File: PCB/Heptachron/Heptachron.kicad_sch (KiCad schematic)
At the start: 37 parts, among them SW1 SW_Push, SW2 SW_Push, U6 BQ24230RGT, U7 IS31FL3729, U8 ATtiny424-SS, X1 RV-3028-C7

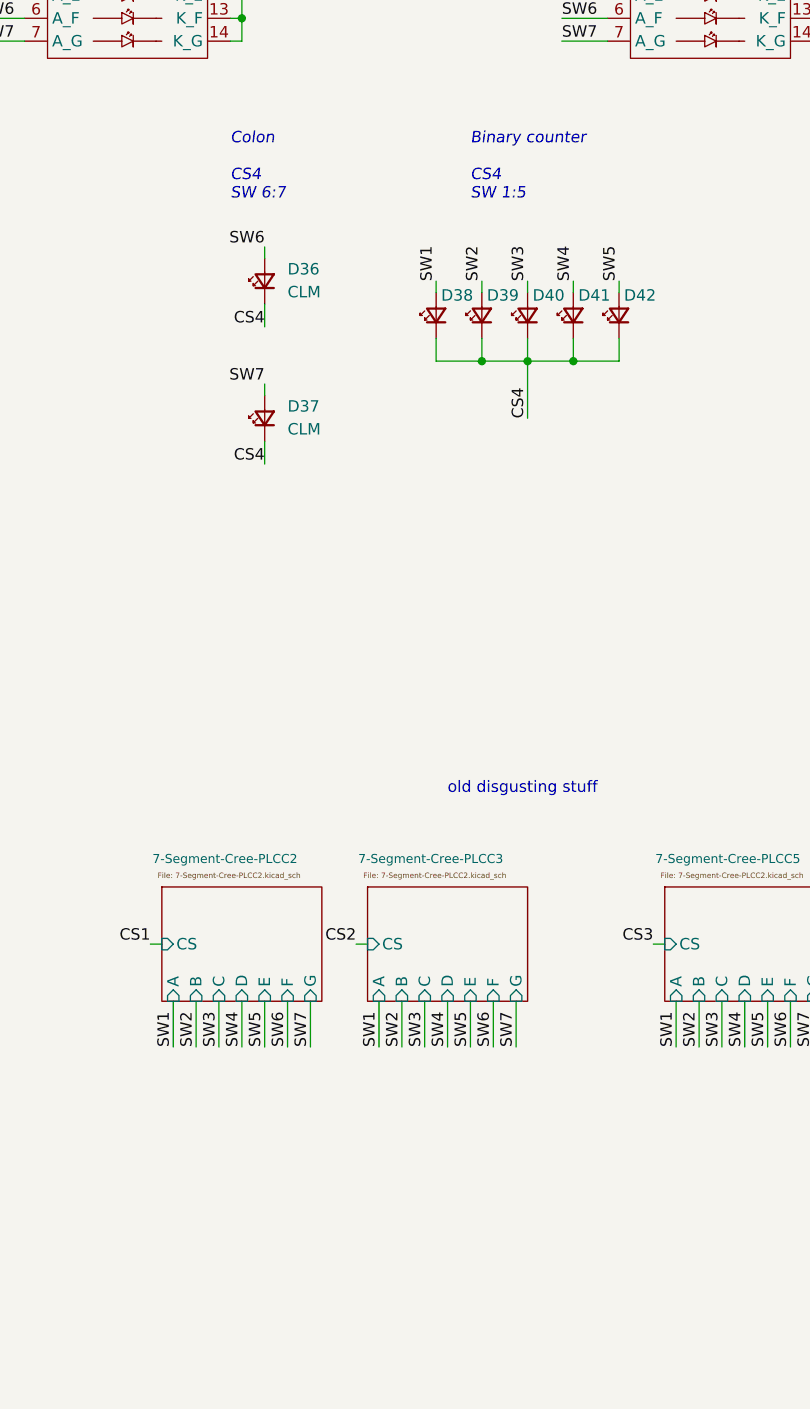
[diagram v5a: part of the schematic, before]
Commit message: Finish test PCB [Ordered]
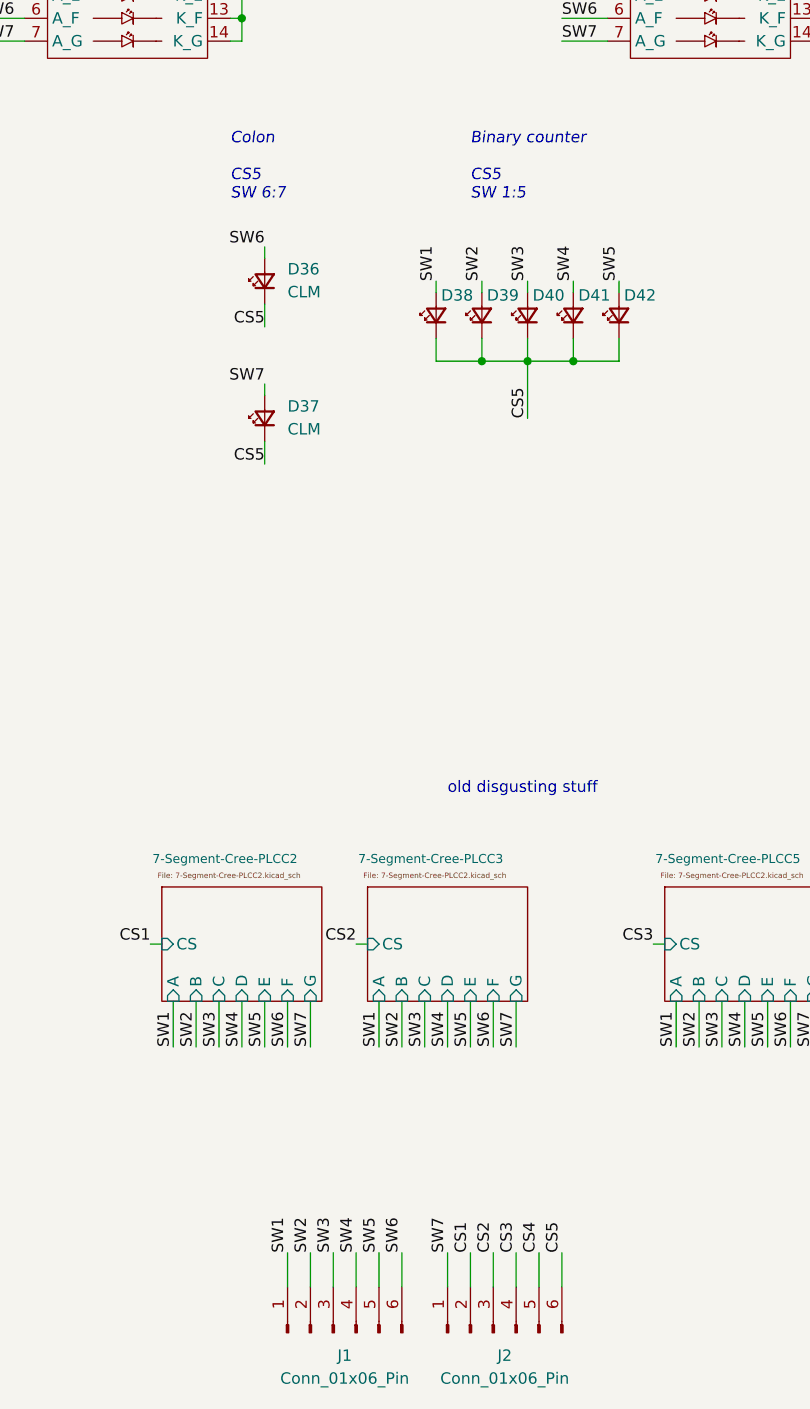
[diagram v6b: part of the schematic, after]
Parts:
- added J1, J2: Conn_01x06_Pin, Connector_Wire:SolderWire-0.1sqmm_1x06_P3.6mm_D0.4mm_OD1mm_Relief, symbol Connector:Conn_01x06_Pin
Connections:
- net CS1: now also J2.2 (Pin_2)
- net CS2: now also J2.3 (Pin_3)
- net CS3: now also J2.4 (Pin_4)
- net CS4: now also J2.5 (Pin_5); no longer D36.1 (K), D37.1 (K), D38.1 (K), D39.1 (K), D40.1 (K), D41.1 (K), D42.1 (K)
- net CS5: now also D36.1 (K), D37.1 (K), D38.1 (K), D39.1 (K), D40.1 (K), D41.1 (K), D42.1 (K), J2.6 (Pin_6)
- net SW1: now also J1.1 (Pin_1)
- net SW2: now also J1.2 (Pin_2)
- net SW3: now also J1.3 (Pin_3)
- net SW4: now also J1.4 (Pin_4)
- net SW5: now also J1.5 (Pin_5)
- net SW6: now also J1.6 (Pin_6)
- net SW7: now also J2.1 (Pin_1)
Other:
- note added: "Binary counter CS5 SW 1:5"
- note added: "Colon CS5 SW 6:7"
- note removed: "Binary counter CS4 SW 1:5"
- note removed: "Colon CS4 SW 6:7"
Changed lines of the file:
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@@
+    (stroke (width 0) (type default))
+  )
+  (wire (pts (xy 311.15 231.14) (xy 311.15 234.95))
     (stroke (width 0) (type default))
   )
@@
     (stroke (width 0) (type default))
   )
+  (wire (pts (xy 331.47 231.14) (xy 331.47 234.95))
+    (stroke (width 0) (type default))
+  )
   (wire (pts (xy 256.54 96.52) (xy 255.27 96.52))
     (stroke (width 0) (type default))
@@
     (stroke (width 0) (type default))
   )
+  (wire (pts (xy 300.99 231.14) (xy 300.99 234.95))
+    (stroke (width 0) (type default))
+  )
   (wire (pts (xy 295.91 91.44) (xy 295.91 93.98))
     (stroke (width 0) (type default))
@@
     (stroke (width 0) (type default))
   )
+  (wire (pts (xy 318.77 231.14) (xy 318.77 234.95))
+    (stroke (width 0) (type default))
+  )
   (wire (pts (xy 295.91 81.28) (xy 295.91 83.82))
     (stroke (width 0) (type default))
@@
     (stroke (width 0) (type default))
   )
+  (wire (pts (xy 303.53 231.14) (xy 303.53 234.95))
+    (stroke (width 0) (type default))
+  )
   (wire (pts (xy 379.73 203.2) (xy 379.73 208.28))
     (stroke (width 0) (type default))
@@
     (stroke (width 0) (type default))
   )
+  (wire (pts (xy 328.93 231.14) (xy 328.93 234.95))
+    (stroke (width 0) (type default))
+  )
   (wire (pts (xy 25.4 62.23) (xy 27.94 62.23))
     (stroke (width 0) (type default))
@@
     (stroke (width 0) (type default))
   )
+  (wire (pts (xy 323.85 231.14) (xy 323.85 234.95))
+    (stroke (width 0) (type default))
+  )
   (wire (pts (xy 29.21 39.37) (xy 25.4 39.37))
     (stroke (width 0) (type default))
@@
     (stroke (width 0) (type default))
   )
+  (wire (pts (xy 321.31 231.14) (xy 321.31 234.95))
+    (stroke (width 0) (type default))
+  )
   (wire (pts (xy 400.05 93.98) (xy 400.05 96.52))
     (stroke (width 0) (type default))
@@
     (stroke (width 0) (type default))
   )
+  (wire (pts (xy 326.39 231.14) (xy 326.39 234.95))
+    (stroke (width 0) (type default))
+  )
   (wire (pts (xy 336.55 88.9) (xy 331.47 88.9))
     (stroke (width 0) (type default))
@@
     (stroke (width 0) (type default))
   )
+  (wire (pts (xy 308.61 231.14) (xy 308.61 234.95))
+    (stroke (width 0) (type default))
+  )
   (wire (pts (xy 67.31 160.02) (xy 64.77 160.02))
     (stroke (width 0) (type default))
@@
     (stroke (width 0) (type default))
   )
+  (wire (pts (xy 313.69 231.14) (xy 313.69 234.95))
+    (stroke (width 0) (type default))
+  )
   (wire (pts (xy 66.04 168.91) (xy 67.31 168.91))
     (stroke (width 0) (type default))
   )
   (wire (pts (xy 130.81 76.2) (xy 129.54 76.2))
+    (stroke (width 0) (type default))
+  )
+  (wire (pts (xy 306.07 231.14) (xy 306.07 234.95))
     (stroke (width 0) (type default))
   )
@@
     (effects (font (size 1.27 1.27)) (justify left bottom))
   )
-  (text "Colon\n\nCS4\nSW 6:7" (at 294.64 114.3 0)
+  (text "Colon\n\nCS5\nSW 6:7" (at 294.64 114.3 0)
     (effects (font (size 1.27 1.27) italic) (justify left bottom))
   )
@@
     (effects (font (size 1.27 1.27)) (justify left bottom))
   )
-  (text "Binary counter\n\nCS4\nSW 1:5" (at 321.31 114.3 0)
+  (text "Binary counter\n\nCS5\nSW 1:5" (at 321.31 114.3 0)
     (effects (font (size 1.27 1.27) italic) (justify left bottom))
   )
@@
     (effects (font (size 1.27 1.27)) (justify left bottom))
   )
+  (label "SW3" (at 306.07 231.14 90) (fields_autoplaced)
+    (effects (font (size 1.27 1.27)) (justify left bottom))
+  )
   (label "CS2" (at 308.61 196.85 180) (fields_autoplaced)
     (effects (font (size 1.27 1.27)) (justify right bottom))
@@
     (effects (font (size 1.27 1.27)) (justify left bottom))
   )
-  (label "CS4" (at 298.45 143.51 180) (fields_autoplaced)
+  (label "CS5" (at 298.45 143.51 180) (fields_autoplaced)
     (effects (font (size 1.27 1.27)) (justify right bottom))
   )
+  (label "CS3" (at 326.39 231.14 90) (fields_autoplaced)
+    (effects (font (size 1.27 1.27)) (justify left bottom))
+  )
   (label "SW1" (at 266.7 81.28 0) (fields_autoplaced)
+    (effects (font (size 1.27 1.27)) (justify left bottom))
+  )
+  (label "SW6" (at 313.69 231.14 90) (fields_autoplaced)
     (effects (font (size 1.27 1.27)) (justify left bottom))
   )
@@
     (effects (font (size 1.27 1.27)) (justify left bottom))
   )
+  (label "CS4" (at 328.93 231.14 90) (fields_autoplaced)
+    (effects (font (size 1.27 1.27)) (justify left bottom))
+  )
+  (label "SW5" (at 311.15 231.14 90) (fields_autoplaced)
+    (effects (font (size 1.27 1.27)) (justify left bottom))
+  )
   (label "CS5" (at 109.22 81.28 180) (fields_autoplaced)
     (effects (font (size 1.27 1.27)) (justify right bottom))
@@
     (effects (font (size 1.27 1.27)) (justify left bottom))
   )
+  (label "CS1" (at 321.31 231.14 90) (fields_autoplaced)
+    (effects (font (size 1.27 1.27)) (justify left bottom))
+  )
   (label "CS6" (at 109.22 83.82 180) (fields_autoplaced)
     (effects (font (size 1.27 1.27)) (justify right bottom))
   )
+  (label "CS2" (at 323.85 231.14 90) (fields_autoplaced)
+    (effects (font (size 1.27 1.27)) (justify left bottom))
+  )
   (label "SW2" (at 129.54 88.9 0) (fields_autoplaced)
     (effects (font (size 1.27 1.27)) (justify left bottom))
@@
     (effects (font (size 1.27 1.27)) (justify left bottom))
   )
+  (label "SW2" (at 303.53 231.14 90) (fields_autoplaced)
+    (effects (font (size 1.27 1.27)) (justify left bottom))
+  )
   (label "SW3" (at 316.23 208.28 90) (fields_autoplaced)
     (effects (font (size 1.27 1.27)) (justify left bottom))
@@
     (effects (font (size 1.27 1.27)) (justify left bottom))
   )
-  (label "CS4" (at 327.66 138.43 90) (fields_autoplaced)
+  (label "CS5" (at 327.66 138.43 90) (fields_autoplaced)
     (effects (font (size 1.27 1.27)) (justify left bottom))
   )
@@
     (effects (font (size 1.27 1.27)) (justify left bottom))
   )
+  (label "CS5" (at 331.47 231.14 90) (fields_autoplaced)
+    (effects (font (size 1.27 1.27)) (justify left bottom))
+  )
   (label "SW1" (at 288.29 208.28 90) (fields_autoplaced)
     (effects (font (size 1.27 1.27)) (justify left bottom))
@@
   )
   (label "SW6" (at 227.33 93.98 0) (fields_autoplaced)
+    (effects (font (size 1.27 1.27)) (justify left bottom))
+  )
+  (label "SW7" (at 318.77 231.14 90) (fields_autoplaced)
     (effects (font (size 1.27 1.27)) (justify left bottom))
   )
@@
     (effects (font (size 1.27 1.27)) (justify left bottom))
   )
-  (label "CS4" (at 298.45 128.27 180) (fields_autoplaced)
+  (label "CS5" (at 298.45 128.27 180) (fields_autoplaced)
     (effects (font (size 1.27 1.27)) (justify right bottom))
   )
@@
     (effects (font (size 1.27 1.27)) (justify left bottom))
   )
+  (label "SW1" (at 300.99 231.14 90) (fields_autoplaced)
+    (effects (font (size 1.27 1.27)) (justify left bottom))
+  )
   (label "SW5" (at 129.54 96.52 0) (fields_autoplaced)
     (effects (font (size 1.27 1.27)) (justify left bottom))
@@
   )
   (label "SW2" (at 369.57 208.28 90) (fields_autoplaced)
+    (effects (font (size 1.27 1.27)) (justify left bottom))
+  )
+  (label "SW4" (at 308.61 231.14 90) (fields_autoplaced)
     (effects (font (size 1.27 1.27)) (justify left bottom))
   )
@@
         (path "/c6ec4407-9aab-4aab-950a-5d337d47ac64"
           (reference "#PWR012") (unit 1)
+        )
+      )
+    )
+  )
+  (symbol (lib_id "Connector:Conn_01x06_Pin") (at 306.07 240.03 90) (unit 1)
+    (in_bom yes) (on_board yes) (dnp no) (fields_autoplaced)
+    (property "Reference" "J1" (at 307.34 242.57 90)
+      (effects (font (size 1.27 1.27)))
+    )
+    (property "Value" "Conn_01x06_Pin" (at 307.34 245.11 90)
+      (effects (font (size 1.27 1.27)))
+    )
+    (property "Footprint" "Connector_Wire:SolderWire-0.1sqmm_1x06_P3.6mm_D0.4mm_OD1mm_Relief" (at 306.07 240.03 0)
+      (effects (font (size 1.27 1.27)) hide)
+    )
+    (property "Datasheet" "~" (at 306.07 240.03 0)
+      (effects (font (size 1.27 1.27)) hide)
+    )
+    (pin "1")
+    (pin "2")
+    (pin "3")
+    (pin "4")
+    (pin "5")
+    (pin "6")
+    (instances
+      (project "Heptachron"
+        (path "/c6ec4407-9aab-4aab-950a-5d337d47ac64"
+          (reference "J1") (unit 1)
         )
       )
@@
         )
       )
+    )
+  )
+  (symbol (lib_id "Connector:Conn_01x06_Pin") (at 323.85 240.03 90) (unit 1)
+    (in_bom yes) (on_board yes) (dnp no) (fields_autoplaced)
+    (property "Reference" "J2" (at 325.12 242.57 90)
+      (effects (font (size 1.27 1.27)))
+    )
+    (property "Value" "Conn_01x06_Pin" (at 325.12 245.11 90)
+      (effects (font (size 1.27 1.27)))
+    )
+    (property "Footprint" "Connector_Wire:SolderWire-0.1sqmm_1x06_P3.6mm_D0.4mm_OD1mm_Relief" (at 323.85 240.03 0)
+      (effects (font (size 1.27 1.27)) hide)
+    )
+    (property "Datasheet" "~" (at 323.85 240.03 0)
+      (effects (font (size 1.27 1.27)) hide)
+    )
+    (pin "1")
+    (pin "2")
+    (pin "3")
+    (pin "4")
+    (pin "5")
+    (pin "6")
+    (instances
+      (project "Heptachron"
+        (path "/c6ec4407-9aab-4aab-950a-5d337d47ac64"
+          (reference "J2") (unit 1)
+        )
+      )

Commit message: Work on schematic
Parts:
- removed D5, D6, D7: CLM, Heptachron-Lib:CREE-PLCC2-custom, symbol Device:LED_Small
- removed J1, J2: Conn_01x06_Pin, Connector_Wire:SolderWire-0.1sqmm_1x06_P3.6mm_D0.4mm_OD1mm_Relief, symbol Connector:Conn_01x06_Pin
- added R10, R11, R12, R9: 1K, symbol Device:R_Small
- added R13, R14: PU, symbol Device:R_Small
- added SW3: SW_DP3T, symbol Switch:SW_DP3T
- D1: value CLM -> PGD; footprint Heptachron-Lib:CREE-PLCC2-custom -> LED_SMD:LED_0603_1608Metric
- D2: value CLM -> CHG; footprint Heptachron-Lib:CREE-PLCC2-custom -> LED_SMD:LED_0603_1608Metric
- D3: value CLM -> BAT; footprint Heptachron-Lib:CREE-PLCC2-custom -> LED_SMD:LED_0603_1608Metric
- D4: value CLM -> VCC; footprint Heptachron-Lib:CREE-PLCC2-custom -> LED_SMD:LED_0603_1608Metric
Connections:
- net +5V: now also SW3.4
- net +BATT: now also R11.2, SW3.2
- net CHG: now also D2.1 (K), U8.2 (PA4)
- net GND: now also D3.1 (K), D4.1 (K), SW1.2, SW2.2
- net LIGHT: now also U8.13 (PA3)
- net PGOOD: now also D1.1 (K), U8.3 (PA5)
- net SCL: now also R14.2
- net SDA: now also R13.2
- net VCC: now also U7.23 (VCC), R10.2, R12.2, R13.1, R14.1, R9.2, SW3.3; no longer C2.2, R3.1, R4.2, U6.10 (OUT), U6.11 (OUT)
- net BU2: now reaches SW2.1
- net BU2: now also U8.5 (PA7)
- net at D1.2 (A): now also R9.1
- net BU1: now reaches SW1.1
- net BU1: now also U8.4 (PA6)
- net at D4.2 (A): now also R12.1
- net TX: now reaches U8.11 (PA1)
- net RX: now reaches U8.12 (PA2)
- net at D3.2 (A): now also R11.1
- net at D2.2 (A): now also R10.1
- new net BMSOUT: C2.2, R3.1, R4.2, SW3.1, U6.10 (OUT), U6.11 (OUT)
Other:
- removed sheet 7-Segment-Cree-PLCC2
- removed sheet 7-Segment-Cree-PLCC3
- removed sheet 7-Segment-Cree-PLCC4
- removed sheet 7-Segment-Cree-PLCC5
- removed sheet 7-segment-subcircuit
- note added: "Ambient light measurement"
- note added: "Battery management"
- note added: "Connectors"
- note added: "Debug LEDs"
- note added: "LED matrix driver"
- note added: "LEDs"
- note added: "MCU - ATtiny424"
- note added: "Pushbuttons"
- note added: "Real Time Clock"
- note added: "System power switch"
- note removed: "old disgusting stuff"
- moved on the sheet: C1, C4, D36, D37, D38, D39, D40, D41, D42, R1, R2, SW1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

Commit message: Update Heptachron.kicad_sch
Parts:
- added R15: 10K, symbol Device:R_Small
- R13, R14: value PU -> 2K
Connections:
- net CS1: now also D38.1 (K), U2.8 (K_A), U3.8 (K_A), U4.8 (K_A); no longer U1.10 (K_C), U1.11 (K_D), U1.12 (K_E), U1.13 (K_F), U1.14 (K_G), U1.9 (K_B)
- net CS2: now also D39.1 (K), U1.9 (K_B), U3.9 (K_B), U4.9 (K_B); no longer U2.10 (K_C), U2.11 (K_D), U2.12 (K_E), U2.13 (K_F), U2.14 (K_G), U2.8 (K_A)
- net CS3: now also D40.1 (K), U1.10 (K_C), U2.10 (K_C), U4.10 (K_C); no longer U3.11 (K_D), U3.12 (K_E), U3.13 (K_F), U3.14 (K_G), U3.8 (K_A), U3.9 (K_B)
- net CS4: now also D41.1 (K), U1.11 (K_D), U2.11 (K_D), U3.11 (K_D); no longer U4.10 (K_C), U4.12 (K_E), U4.13 (K_F), U4.14 (K_G), U4.8 (K_A), U4.9 (K_B)
- net CS5: now also U1.12 (K_E), U2.12 (K_E), U3.12 (K_E), U4.12 (K_E); no longer D36.1 (K), D37.1 (K), D38.1 (K), D39.1 (K), D40.1 (K), D41.1 (K)
- net CS6: now also D37.1 (K), U1.13 (K_F), U2.13 (K_F), U3.13 (K_F), U4.13 (K_F)
- net CS7: now also D36.1 (K), U1.14 (K_G), U2.14 (K_G), U3.14 (K_G), U4.14 (K_G)
- net GND: now also R15.1
- net SW1: now also U1.2 (A_B), U1.3 (A_C), U1.4 (A_D), U1.5 (A_E), U1.6 (A_F), U1.7 (A_G); no longer D38.2 (A), U2.1 (A_A), U3.1 (A_A), U4.1 (A_A)
- net SW2: now also U2.1 (A_A), U2.3 (A_C), U2.4 (A_D), U2.5 (A_E), U2.6 (A_F), U2.7 (A_G); no longer D39.2 (A), U1.2 (A_B), U3.2 (A_B), U4.2 (A_B)
- net SW3: now also U3.1 (A_A), U3.2 (A_B), U3.4 (A_D), U3.5 (A_E), U3.6 (A_F), U3.7 (A_G); no longer D40.2 (A), U1.3 (A_C), U2.3 (A_C), U4.3 (A_C)
- net SW4: now also U4.1 (A_A), U4.2 (A_B), U4.3 (A_C), U4.5 (A_E), U4.6 (A_F), U4.7 (A_G); no longer D41.2 (A), U1.4 (A_D), U2.4 (A_D), U3.4 (A_D)
- net SW5: now also D36.2 (A), D37.2 (A), D38.2 (A), D39.2 (A), D40.2 (A), D41.2 (A); no longer U1.5 (A_E), U2.5 (A_E), U3.5 (A_E), U4.5 (A_E)
- net LED_EN: now reaches U8.7 (PB2)
- net LED_EN: now also U7.29 (SDB)
- net at U7.25 (ISET): now also R15.2
- removed net SW6: D36.2 (A), U1.6 (A_F), U2.6 (A_F), U3.6 (A_F), U4.6 (A_F), U7.17 (SW6)
- removed net SW7: D37.2 (A), U1.7 (A_G), U2.7 (A_G), U3.7 (A_G), U4.7 (A_G), U7.16 (SW7)
- net SW8: no longer names the net of U7.15 (SW8)
- no-connect marks 2 -> 14
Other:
- note added: "QFP available"
